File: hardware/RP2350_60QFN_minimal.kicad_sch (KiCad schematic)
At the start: 54 parts, among them J1 UJ20-C-H-G-SMT-2A-P16-TR, J4 SM03B-SRSS-TB, J5 4677, SW1 SW_Push, SW2 SW_Push, U1 RP2350_60QFN, U2 MIC5205-3.3YM5, U3 W25Q128JVS, U4 LM27762, Y1 ABM8-272-T3

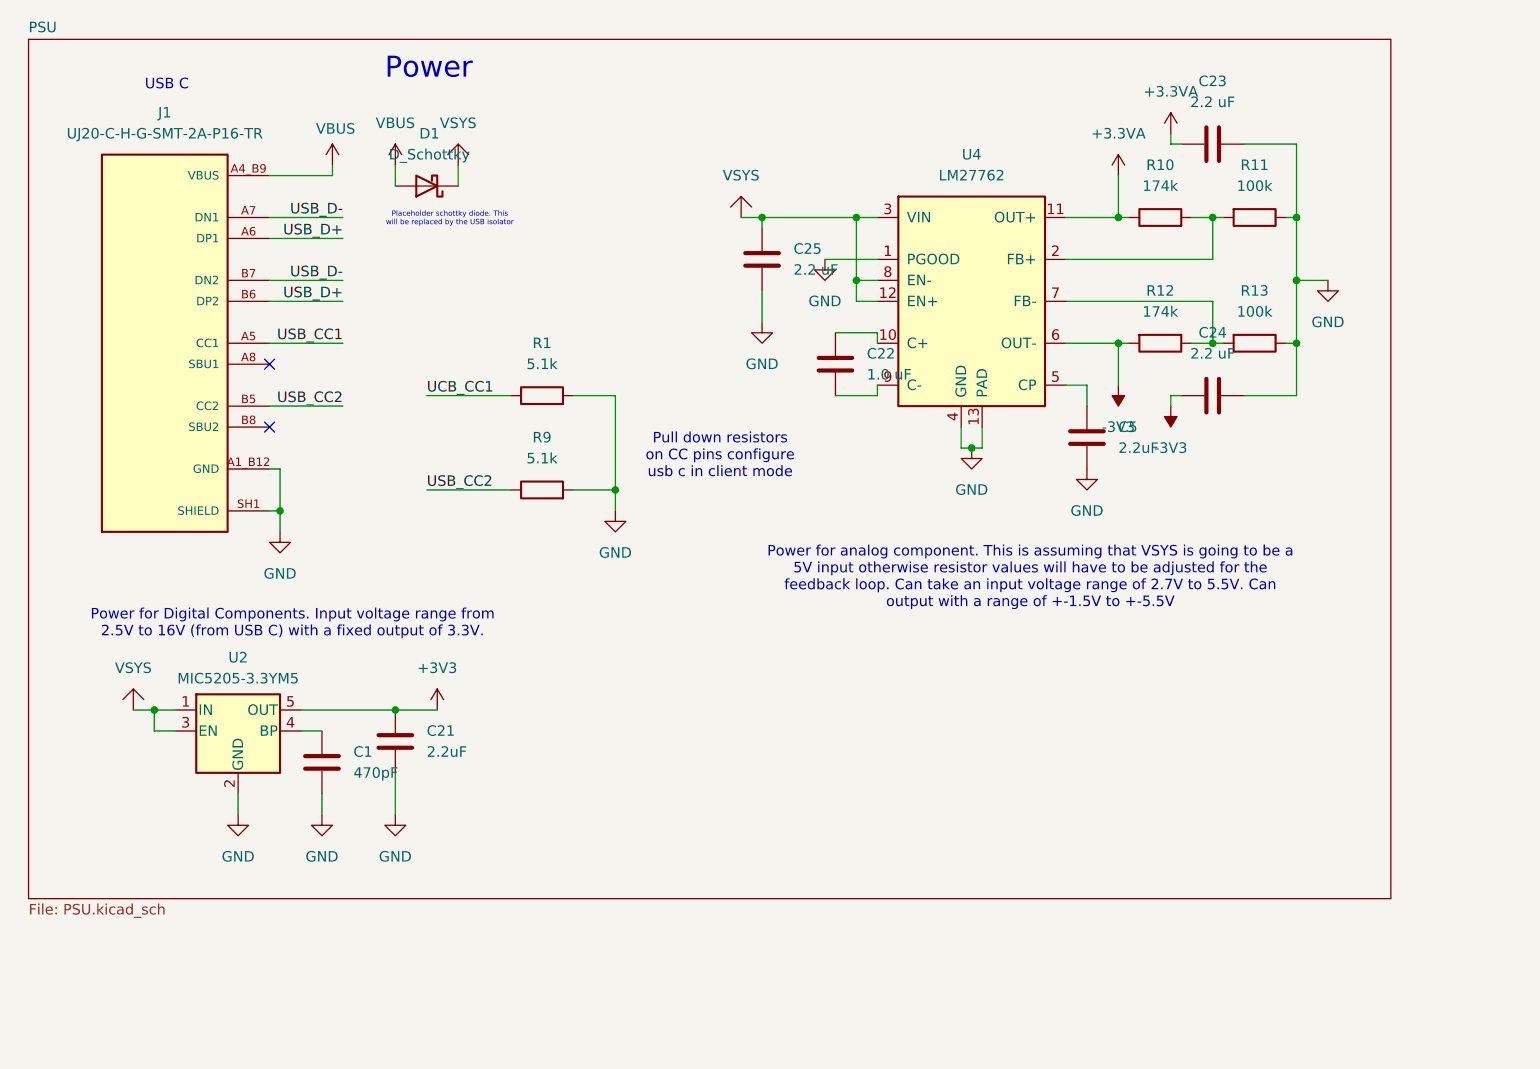
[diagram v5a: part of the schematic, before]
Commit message: feat(hardware): Move PSU to subschematic
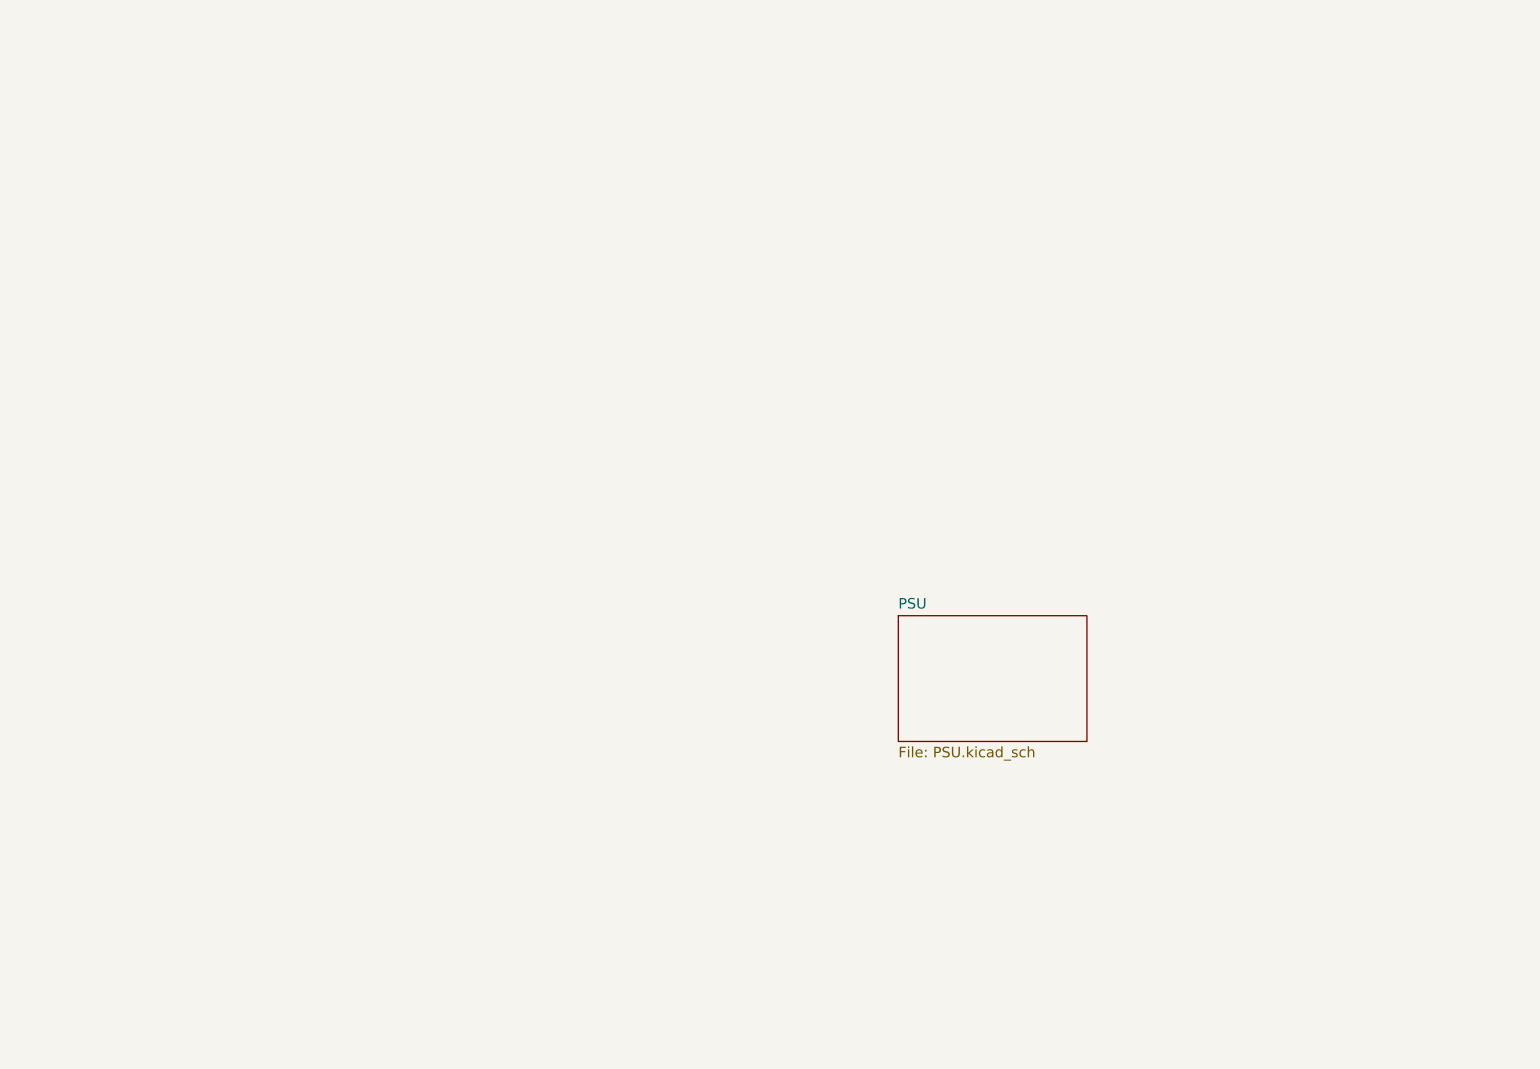
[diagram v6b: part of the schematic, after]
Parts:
- removed C1: 470pF, symbol Device:C
- removed C21, C5: 2.2uF, symbol Device:C
- removed C22: 1.0 uF, symbol Device:C
- removed C23, C24, C25: 2.2 uF, symbol Device:C
- removed D1: D_Schottky, symbol Device:D_Schottky
- removed J1: UJ20-C-H-G-SMT-2A-P16-TR, UJ20-C-H-G-SMT-1-P16-TR:SAMESKY_UJ20-C-H-G-SMT-1-P16-TR, symbol UJ20-C-H-G-SMT-1-P16-TR:UJ20-C-H-G-SMT-1-P16-TR
- removed R1, R9: 5.1k, symbol Device:R
- removed R10, R12: 174k, symbol Device:R
- removed R11, R13: 100k, symbol Device:R
- removed U2: MIC5205-3.3YM5, Package_TO_SOT_SMD:SOT-23-5, symbol Regulator_Linear:MIC5205-3.3YM5
- removed U4: LM27762, Package_SON:WSON-12-1EP_3x2mm_P0.5mm_EP1x2.65_ThermalVias, symbol Regulator_SwitchedCapacitor:LM27762
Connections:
- no-connect marks 2 -> 0
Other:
- note removed: "Placeholder schottky diode. This will be replaced by the USB isolator"
- note removed: "Power"
- note removed: "Power for Digital Components. Input voltage range from 2.5V to 16V (from USB C) with a fixed output of 3.3V."
- note removed: "Power for analog component. This is assuming that VSYS is going to be a 5V input otherwise resistor values will have to be adjusted for the feedback loop. Can take an input voltage range of 2.7V to 5.5V. Can output with a range of +-1.5V to +-5.5V"
- note removed: "Pull down resistors on CC pins configure usb c in client mode"
- note removed: "USB C"

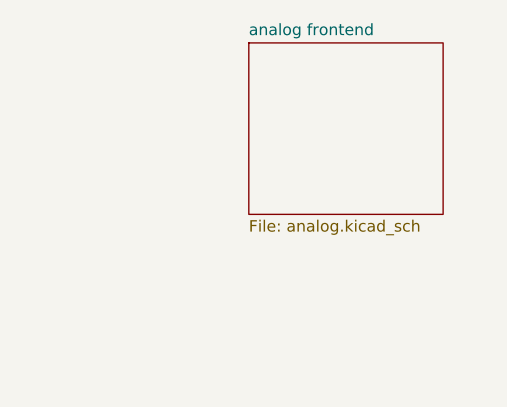
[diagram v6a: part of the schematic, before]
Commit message: added heirarchical labels for analog block
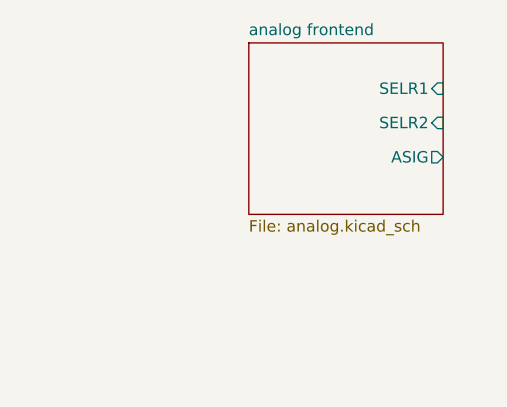
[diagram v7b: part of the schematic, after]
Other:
- sheet analog frontend ports: added ASIG, SELR1, SELR2; removed none
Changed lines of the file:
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@@
+			)
+		)
+		(pin "SELR1" input
+			(at 453.39 78.74 0)
+			(effects
+				(font
+					(size 1.27 1.27)
+				)
+				(justify right)
+			)
+		)
+		(pin "ASIG" output
+			(at 453.39 86.36 0)
+			(effects
+				(font
+					(size 1.27 1.27)
+				)
+				(justify right)
+			)
+		)
+		(pin "SELR2" input
+			(at 453.39 82.55 0)
+			(effects
+				(font
+					(size 1.27 1.27)
+				)
+				(justify right)
 			)
 		)

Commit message: Up to date
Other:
- added sheet Trigger (Trigger.kicad_sch)
- sheet PSU ports: added -1V65, 1V65, VREF, VSYS; removed none
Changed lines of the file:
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@@
+			)
+		)
+		(pin "-1V65" output
+			(at 143.51 88.9 0)
+			(effects
+				(font
+					(size 1.27 1.27)
+				)
+				(justify right)
+			)
+		)
+		(pin "1V65" output
+			(at 143.51 91.44 0)
+			(effects
+				(font
+					(size 1.27 1.27)
+				)
+				(justify right)
+			)
+		)
+		(pin "VREF" output
+			(at 143.51 93.98 0)
+			(effects
+				(font
+					(size 1.27 1.27)
+				)
+				(justify right)
+			)
+		)
+		(pin "VSYS" output
+			(at 143.51 96.52 0)
+			(effects
+				(font
+					(size 1.27 1.27)
+				)
+				(justify right)
 			)
 		)
@@
 				)
 			)
+		)
+	)
+	(sheet
+		(at 189.23 44.45)
+		(size 27.94 15.24)
+		(exclude_from_sim no)
+		(in_bom yes)
+		(on_board yes)
+		(dnp no)
+		(fields_autoplaced yes)
+		(stroke
+			(width 0.1524)
+			(type solid)
+		)
+		(fill
+			(color 0 0 0 0.0000)
+		)
+		(property "Sheetname" "Trigger"
+			(at 189.23 43.7384 0)
+			(effects
+				(font
+					(size 1.27 1.27)
+				)
+				(justify left bottom)
+			)
+		)
+		(property "Sheetfile" "Trigger.kicad_sch"
+			(at 189.23 60.2746 0)
+			(effects
+				(font
+					(size 1.27 1.27)
+				)
+				(justify left top)
+			)
+		)
+		(instances
+			(project "RP2350_60QFN_minimal"
+				(path "/94683f5c-9cd9-448e-be96-9792537b5cb8"
+					(page "4")
+				)
+			)
